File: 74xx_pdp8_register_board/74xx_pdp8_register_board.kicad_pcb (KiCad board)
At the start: 4 copper layers, 149.9 x 88.9 mm, 39 parts, among them P1 DIL24, P2 DIL24, P3 DIL24, P4 DIL24, P5 DIL24, U1 74HC125, U10 74HC04, U11 74HC163, U12 74HC163, U13 74HC163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

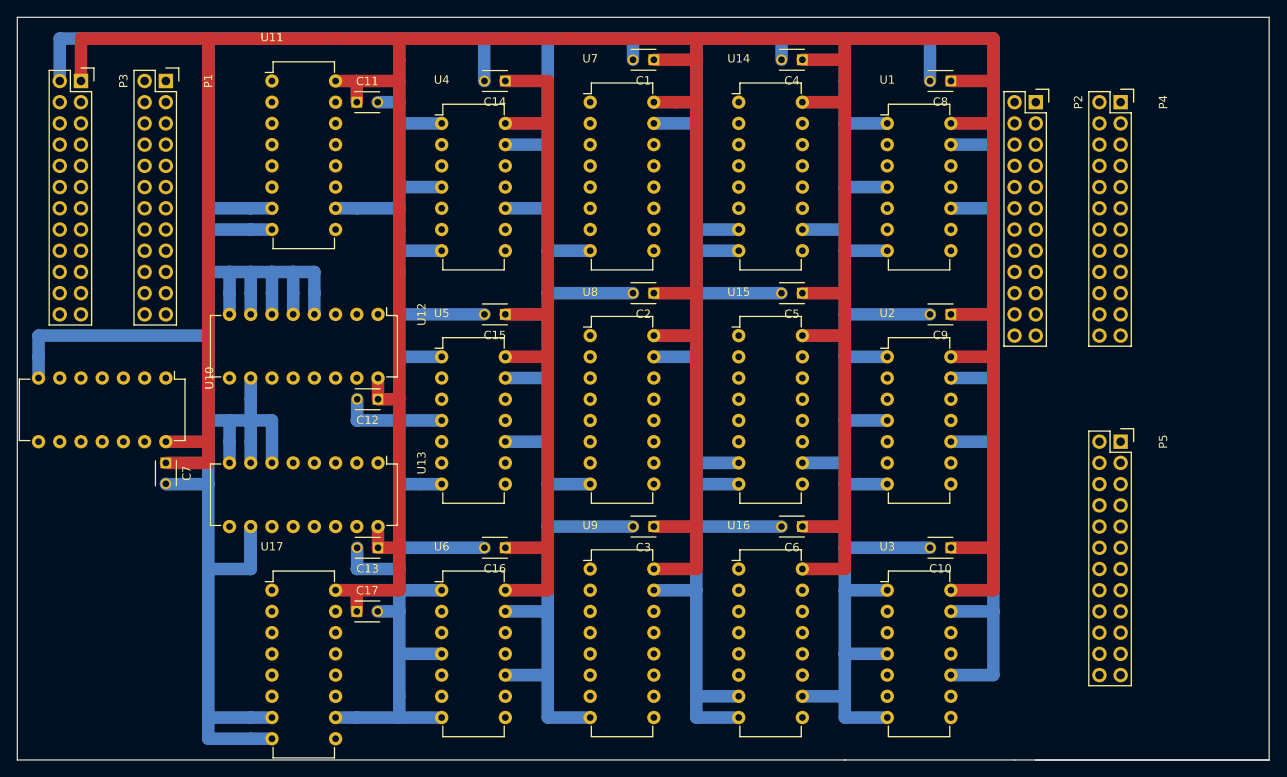
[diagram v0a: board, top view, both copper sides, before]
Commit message: Roughed-out layout of register multiplexor board. Need to double check dimensions of twin register board.
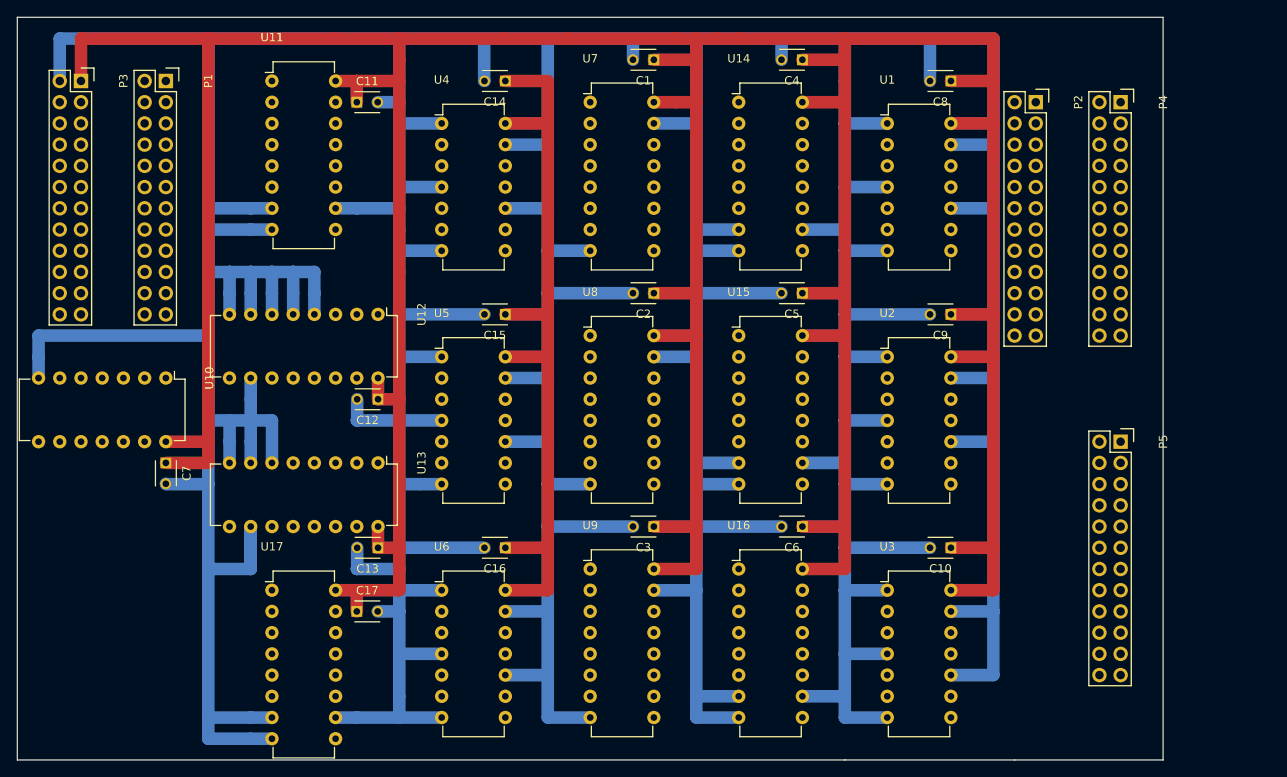
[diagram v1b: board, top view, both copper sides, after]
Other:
- board size 149.9 x 88.9 mm -> 137.2 x 88.9 mm
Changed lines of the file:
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@@
     (links 262)
     (no_connects 154)
-    (area 17.704999 104.064999 167.715001 193.115001)
+    (area 17.634999 104.064999 167.715001 193.195001)
     (thickness 1.6)
-    (drawings 7)
+    (drawings 6)
     (tracks 562)
     (zones 0)
@@
   )
   (setup
-    (last_trace_width 1.5)
+    (last_trace_width 0.25)
     (user_trace_width 0.5)
     (user_trace_width 1)
@@
     )
   )
+  (gr_line (start 154.94 193.04) (end 137.16 193.04) (angle 90) (layer Edge.Cuts) (width 0.15))
+  (gr_line (start 154.94 104.14) (end 154.94 193.04) (angle 90) (layer Edge.Cuts) (width 0.15))
+  (gr_line (start 17.78 104.14) (end 154.94 104.14) (angle 90) (layer Edge.Cuts) (width 0.15))
   (gr_line (start 17.78 104.14) (end 17.78 193.04) (angle 90) (layer Edge.Cuts) (width 0.15))
-  (gr_line (start 139.7 193.04) (end 167.64 193.04) (angle 90) (layer Edge.Cuts) (width 0.15))
-  (gr_line (start 167.64 193.04) (end 137.16 193.04) (angle 90) (layer Edge.Cuts) (width 0.15))
-  (gr_line (start 167.64 104.14) (end 167.64 193.04) (angle 90) (layer Edge.Cuts) (width 0.15))
-  (gr_line (start 17.78 104.14) (end 167.64 104.14) (angle 90) (layer Edge.Cuts) (width 0.15))
   (gr_line (start 116.84 193.04) (end 137.16 193.04) (angle 90) (layer Edge.Cuts) (width 0.15))
   (gr_line (start 116.84 193.04) (end 17.78 193.04) (angle 90) (layer Edge.Cuts) (width 0.15))
